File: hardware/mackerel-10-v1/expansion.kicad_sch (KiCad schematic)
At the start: 0 parts

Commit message: Mostly routed except expansion
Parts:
- added J9: Conn_02x20_Odd_Even, Connector_IDC:IDC-Header_2x20_P2.54mm_Vertical, symbol Connector_Generic:Conn_02x20_Odd_Even
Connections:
- net +5V: now also J9.1 (Pin_1), J9.2 (Pin_2)
- net A1: now also J9.13 (Pin_13)
- net A10: now also J9.24 (Pin_24)
- net A11: now also J9.25 (Pin_25)
- net A12: now also J9.26 (Pin_26)
- net A13: now also J9.27 (Pin_27)
- net A14: now also J9.28 (Pin_28)
- net A15: now also J9.29 (Pin_29)
- net A2: now also J9.14 (Pin_14)
- net A3: now also J9.15 (Pin_15)
- net A4: now also J9.16 (Pin_16)
- net A5: now also J9.17 (Pin_17)
- net A6: now also J9.18 (Pin_18)
- net A7: now also J9.19 (Pin_19)
- net A8: now also J9.20 (Pin_20)
- net A9: now also J9.23 (Pin_23)
- net D0: now also J9.5 (Pin_5)
- net D1: now also J9.6 (Pin_6)
- net D2: now also J9.7 (Pin_7)
- net D3: now also J9.8 (Pin_8)
- net D4: now also J9.9 (Pin_9)
- net D5: now also J9.10 (Pin_10)
- net D6: now also J9.11 (Pin_11)
- net D7: now also J9.12 (Pin_12)
- net GND: now also J9.21 (Pin_21), J9.22 (Pin_22), J9.3 (Pin_3), J9.4 (Pin_4)
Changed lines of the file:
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@@
+	)
+	(symbol
+		(lib_id "Connector_Generic:Conn_02x20_Odd_Even")
+		(at 76.2 73.66 0)
+		(unit 1)
+		(exclude_from_sim no)
+		(in_bom yes)
+		(on_board yes)
+		(dnp no)
+		(fields_autoplaced yes)
+		(property "Reference" "J9"
+			(at 77.47 44.45 0)
+			(effects
+				(font
+					(size 1.27 1.27)
+				)
+			)
+		)
+		(property "Value" "Conn_02x20_Odd_Even"
+			(at 77.47 46.99 0)
+			(effects
+				(font
+					(size 1.27 1.27)
+				)
+				(hide yes)
+			)
+		)
+		(property "Footprint" "Connector_IDC:IDC-Header_2x20_P2.54mm_Vertical"
+			(at 76.2 73.66 0)
+			(effects
+				(font
+					(size 1.27 1.27)
+				)
+				(hide yes)
+			)
+		)
+		(property "Datasheet" "~"
+			(at 76.2 73.66 0)
+			(effects
+				(font
+					(size 1.27 1.27)
+				)
+				(hide yes)
+			)
+		)
+		(property "Description" "Generic connector, double row, 02x20, odd/even pin numbering scheme (row 1 odd numbers, row 2 even numbers), script generated (kicad-library-utils/schlib/autogen/connector/)"
+			(at 76.2 73.66 0)
+			(effects
+				(font
+					(size 1.27 1.27)
+				)
+				(hide yes)
+			)
+		)
+		(pin "27"
+		)
+		(pin "39"
+		)
+		(pin "18"
+		)
+		(pin "26"
+		)
+		(pin "29"
+		)
+		(pin "9"
+		)
+		(pin "40"
+		)
+		(pin "20"
+		)
+		(pin "19"
+		)
+		(pin "21"
+		)
+		(pin "37"
+		)
+		(pin "24"
+		)
+		(pin "34"
+		)
+		(pin "33"
+		)
+		(pin "35"
+		)
+		(pin "14"
+		)
+		(pin "23"
+		)
+		(pin "32"
+		)
+		(pin "3"
+		)
+		(pin "22"
+		)
+		(pin "17"
+		)
+		(pin "25"
+		)
+		(pin "30"
+		)
+		(pin "7"
+		)
+		(pin "38"
+		)
+		(pin "8"
+		)
+		(pin "4"
+		)
+		(pin "6"
+		)
+		(pin "5"
+		)
+		(pin "36"
+		)
+		(pin "12"
+		)
+		(pin "13"
+		)
+		(pin "10"
+		)
+		(pin "11"
+		)
+		(pin "1"
+		)
+		(pin "2"
+		)
+		(pin "31"
+		)
+		(pin "16"
+		)
+		(pin "15"
+		)
+		(pin "28"
+		)
+		(instances
+			(project "mackerel-10-v1"
+				(path "/0a8f74be-008b-4256-a2d9-73a458311ea0/eb382f11-e263-426f-affb-26cce29b45e2"
+					(reference "J9")
+					(unit 1)
+				)
+			)
+		)
 	)
 	(symbol

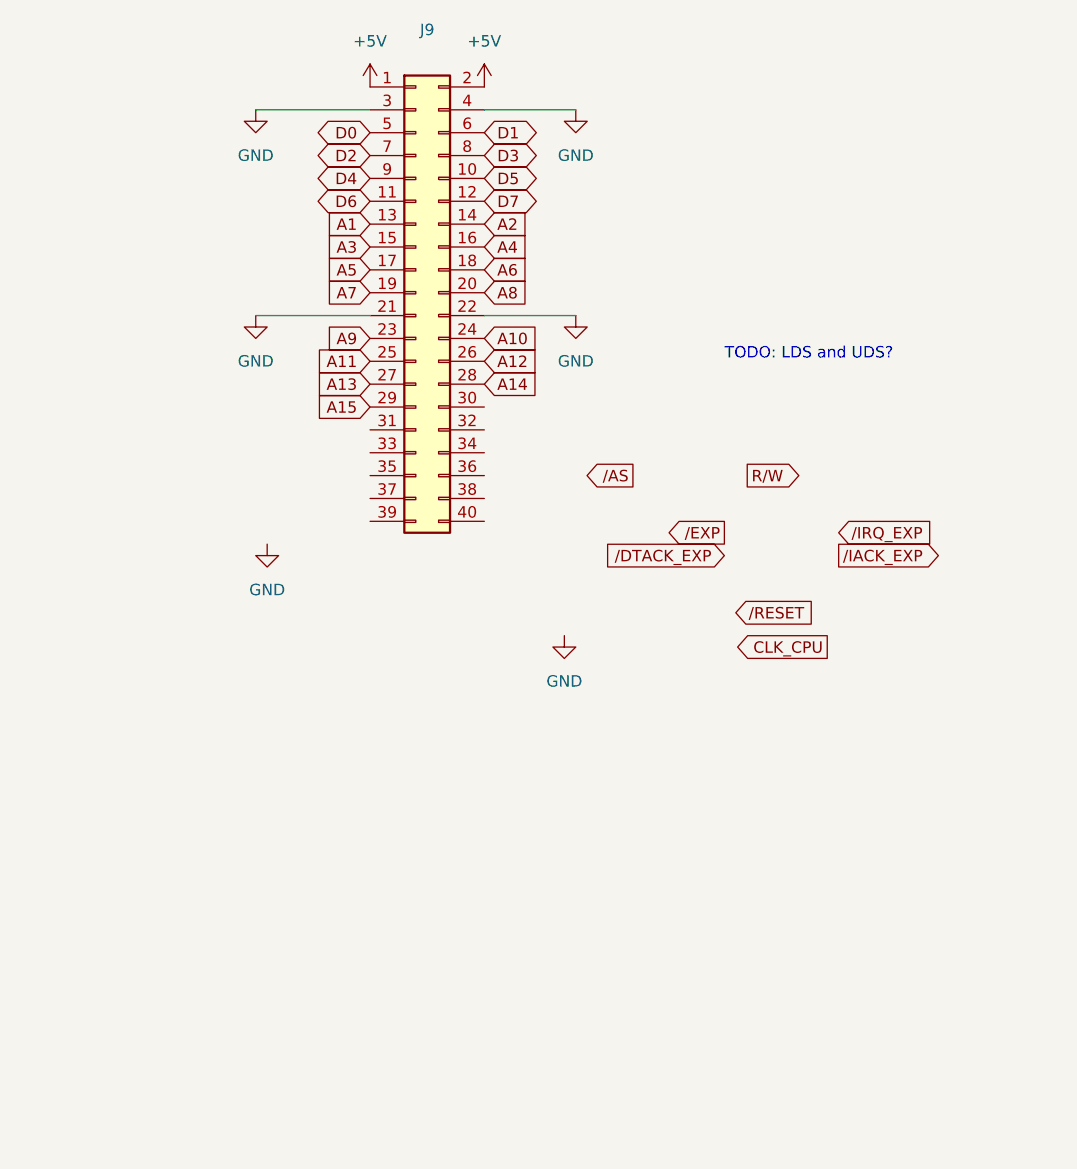
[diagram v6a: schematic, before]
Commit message: IDE interface routed
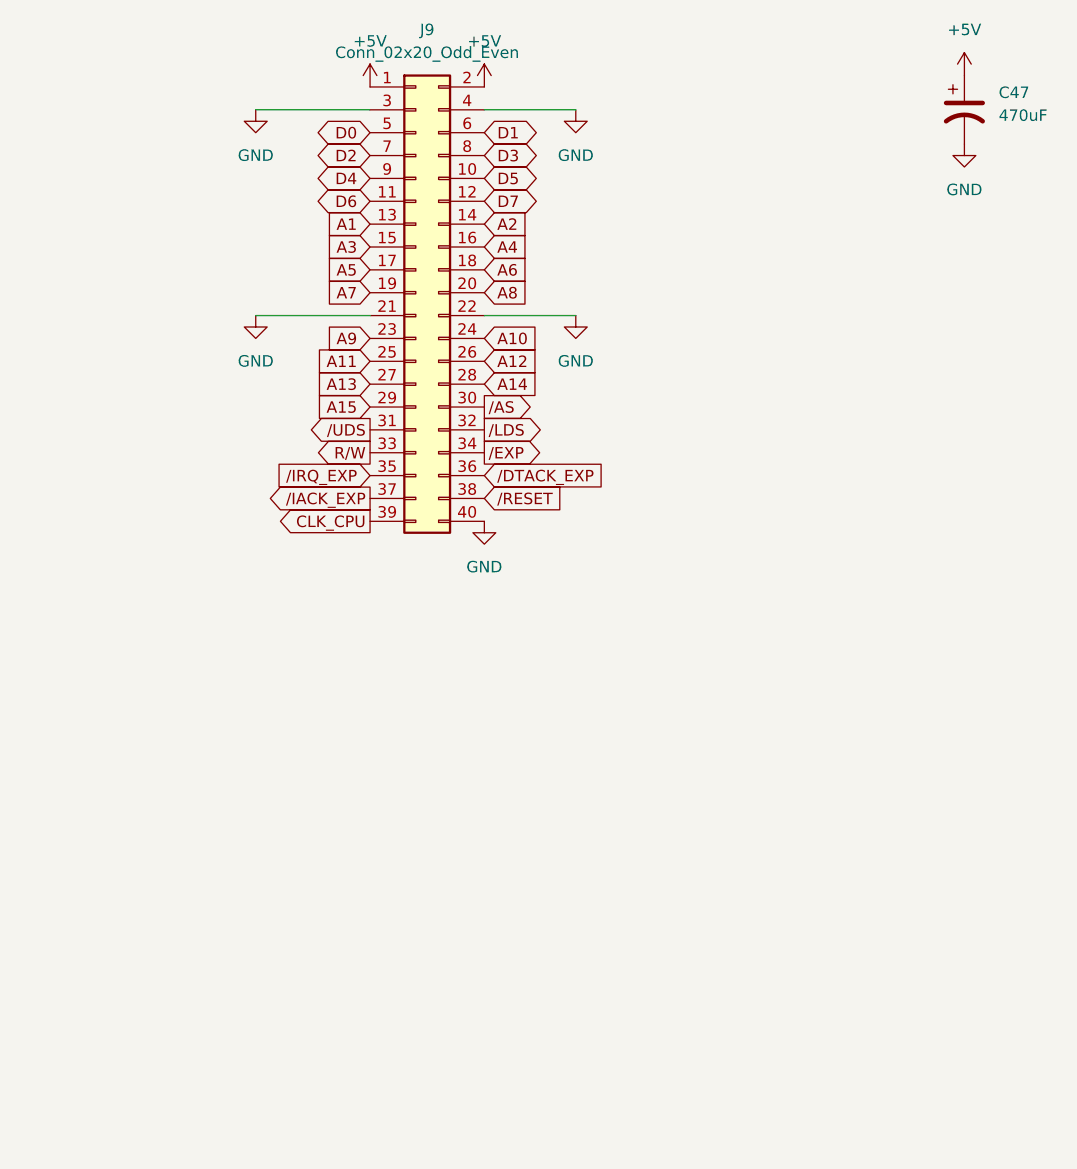
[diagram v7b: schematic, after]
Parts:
- added C47: 470uF, Capacitor_THT:CP_Radial_D8.0mm_P3.50mm, symbol Device:C_Polarized_US
- J9: footprint Connector_IDC:IDC-Header_2x20_P2.54mm_Vertical -> Connector_PinHeader_2.54mm:PinHeader_2x20_P2.54mm_Vertical
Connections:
- net +5V: now also C47.1
- net CLK_CPU: now also J9.39 (Pin_39)
- net GND: now also J9.40 (Pin_40), C47.2
- net R/W: now also J9.33 (Pin_33)
- net /AS: now also J9.30 (Pin_30)
- net /DTACK_EXP: now also J9.36 (Pin_36)
- net /EXP: now also J9.34 (Pin_34)
- net /IACK_EXP: now also J9.37 (Pin_37)
- net /IRQ_EXP: now also J9.35 (Pin_35)
- net /RESET: now also J9.38 (Pin_38)
- net /UDS: now reaches J9.31 (Pin_31)
- net /LDS: now reaches J9.32 (Pin_32)
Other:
- note removed: "TODO: LDS and UDS?"

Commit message: Mack-10 v1 fully routed
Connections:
- net A1: now also J9.23 (Pin_23); no longer J9.13 (Pin_13)
- net A10: now also J9.34 (Pin_34); no longer J9.24 (Pin_24)
- net A11: now also J9.33 (Pin_33); no longer J9.25 (Pin_25)
- net A12: now also J9.36 (Pin_36); no longer J9.26 (Pin_26)
- net A13: now also J9.35 (Pin_35); no longer J9.27 (Pin_27)
- net A14: now also J9.38 (Pin_38); no longer J9.28 (Pin_28)
- net A15: now also J9.37 (Pin_37); no longer J9.29 (Pin_29)
- net A2: now also J9.26 (Pin_26); no longer J9.14 (Pin_14)
- net A3: now also J9.25 (Pin_25); no longer J9.15 (Pin_15)
- net A4: now also J9.28 (Pin_28); no longer J9.16 (Pin_16)
- net A5: now also J9.27 (Pin_27); no longer J9.17 (Pin_17)
- net A6: now also J9.30 (Pin_30); no longer J9.18 (Pin_18)
- net A7: now also J9.29 (Pin_29); no longer J9.19 (Pin_19)
- net A8: now also J9.32 (Pin_32); no longer J9.20 (Pin_20)
- net A9: now also J9.31 (Pin_31); no longer J9.23 (Pin_23)
- net CLK_CPU: now also J9.24 (Pin_24); no longer J9.39 (Pin_39)
- net D0: now also J9.9 (Pin_9); no longer J9.5 (Pin_5)
- net D1: now also J9.10 (Pin_10); no longer J9.6 (Pin_6)
- net D2: now also J9.11 (Pin_11); no longer J9.7 (Pin_7)
- net D3: now also J9.12 (Pin_12); no longer J9.8 (Pin_8)
- net D4: now also J9.13 (Pin_13); no longer J9.9 (Pin_9)
- net D5: now also J9.14 (Pin_14); no longer J9.10 (Pin_10)
- net D6: now also J9.15 (Pin_15); no longer J9.11 (Pin_11)
- net D7: now also J9.16 (Pin_16); no longer J9.12 (Pin_12)
- net R/W: now also J9.19 (Pin_19); no longer J9.33 (Pin_33)
- net /AS: now also J9.18 (Pin_18); no longer J9.30 (Pin_30)
- net /DTACK_EXP: now also J9.8 (Pin_8); no longer J9.36 (Pin_36)
- net /EXP: now also J9.6 (Pin_6); no longer J9.34 (Pin_34)
- net /IACK_EXP: now also J9.7 (Pin_7); no longer J9.37 (Pin_37)
- net /IRQ_EXP: now also J9.5 (Pin_5); no longer J9.35 (Pin_35)
- net /LDS: now also J9.20 (Pin_20); no longer J9.32 (Pin_32)
- net /RESET: now also J9.39 (Pin_39); no longer J9.38 (Pin_38)
- net /UDS: now also J9.17 (Pin_17); no longer J9.31 (Pin_31)
